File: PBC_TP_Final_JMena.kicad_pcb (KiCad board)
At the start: 2 copper layers, 60 x 96 mm, 146 parts, among them J201 Barrel_Jack, J301 Conn_01x02_Female, J302 Conn_01x02_Female, J303 Conn_01x02_Female, J304 Conn_01x02_Female, J305 Conn_01x02_Female, J306 Conn_01x02_Female, J307 Conn_01x02_Female, J308 Conn_01x02_Female, J501 Conn_01x40_Male, J502 Conn_01x40_Male, J503 Conn_01x06_Male, J504 Conn_01x04, J505 Conn_01x04, J601 USB_B_Micro, J602 DB9_Male, Q401 FDV301N, Q402 FDV301N, Q403 FDV301N, Q404 FDV301N, Q405 FDV301N, Q406 FDV301N, Q407 FDV301N, Q408 FDV301N, Q501 FDV301N, Q502 FDV301N, Q503 FDV301N, Q504 FDV301N, Q505 FDV301N, Q506 FDV301N, Q507 FDV301N, Q508 FDV301N, SW201 SW_DIP_x01, SW401 SW_Push, SW402 SW_Push, SW403 SW_Push, SW404 SW_Push, SW405 SW_Push, SW406 SW_Push, SW407 SW_Push, SW408 SW_Push, U201 NCP1117-5.0_SOT223, U202 LM1084-3.3, U301 LM324, U302 LM324, U303 ADS7828, U304 MCP1525-TT, U601 FT232RL, U602 MAX3232

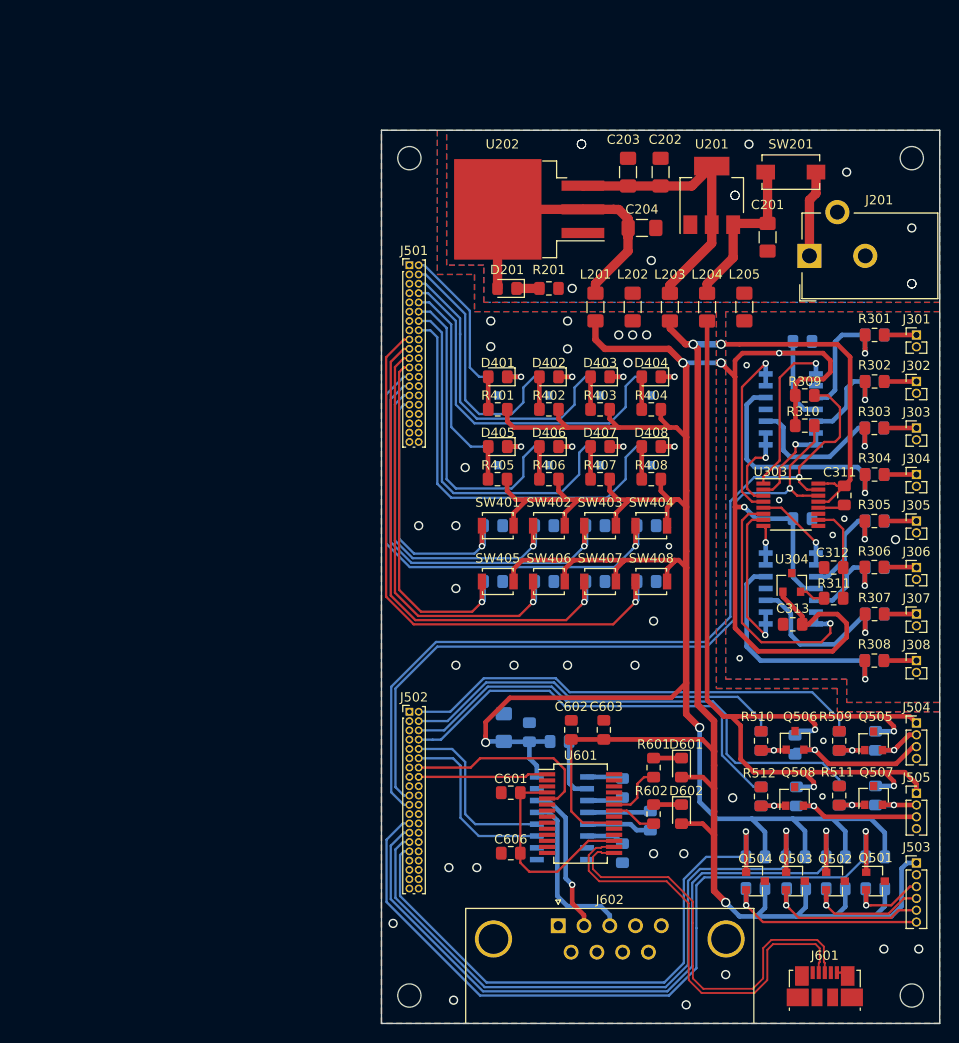
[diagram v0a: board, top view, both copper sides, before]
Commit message: Se realizan correcciones finales y se agregan carpetas BOM, Datasheet, Doc, Gerbers, lib.pretty y shapes3D
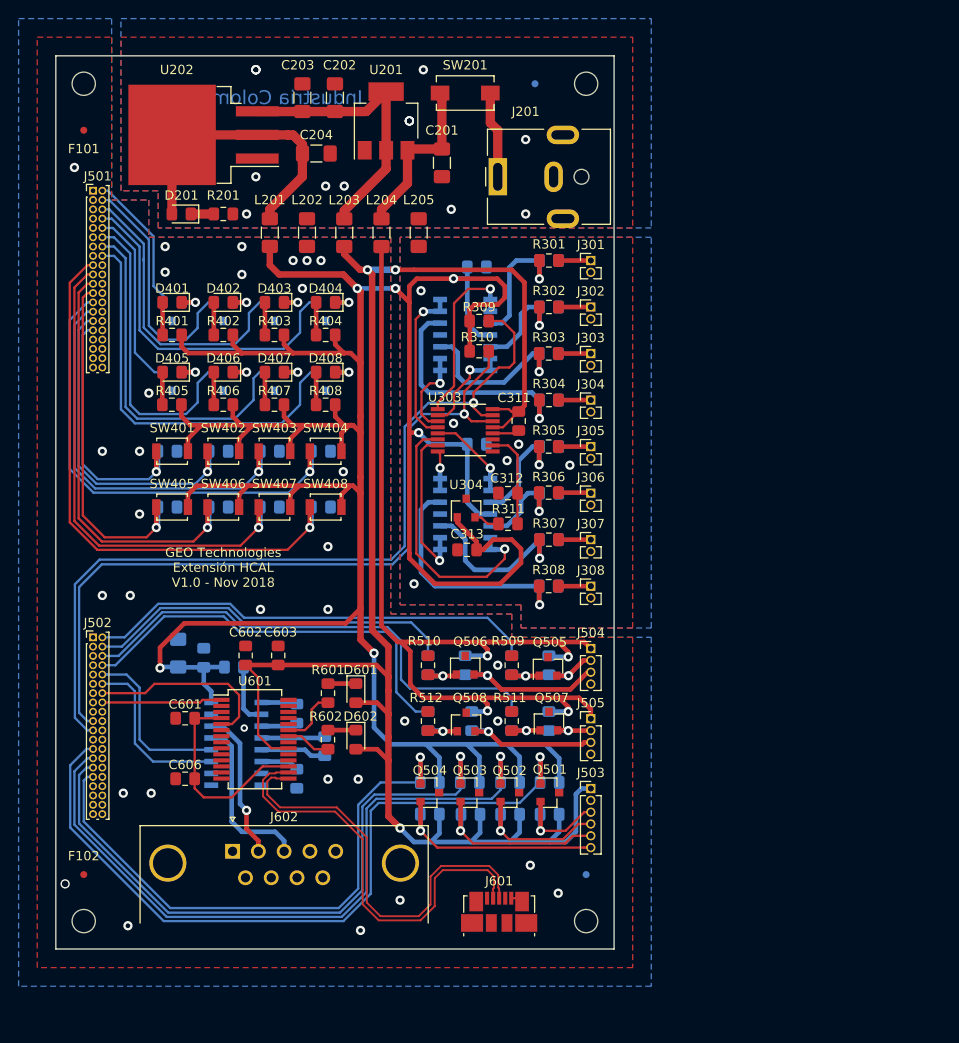
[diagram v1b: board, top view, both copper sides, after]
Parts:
- added F101: Fiducial, Fiducial:Fiducial_0.75mm_Dia_1.5mm_Outer, F.Cu at (82.0, 60.0)
- added F102: Fiducial, Fiducial:Fiducial_0.75mm_Dia_1.5mm_Outer, F.Cu at (82.0, 140.0)
- added F103: Fiducial, Fiducial:Fiducial_0.75mm_Dia_1.5mm_Outer, B.Cu at (130.5, 55.0)
- added F104: Fiducial, Fiducial:Fiducial_0.75mm_Dia_1.5mm_Outer, B.Cu at (136.0, 140.0)
- J201: footprint Connector_BarrelJack:BarrelJack_CUI_PJ-102AH_Horizontal -> Connector_BarrelJack:BarrelJack_CUI_PJ-063AH_Horizontal
- J602: footprint Connector_Dsub:DSUB-9_Male_Horizontal_P2.77x2.84mm_EdgePinOffset7.70mm_Housed_MountingHolesOffset9.12mm -> Connector_Dsub:DSUB-9_Male_Horizontal_P2.77x2.84mm_EdgePinOffset4.94mm_Housed_MountingHolesOffset7.48mm
- moved R506 36.7 mm to (119.0, 117.5)
- moved R510 36.7 mm to (119.0, 117.5)
- moved R508 36.7 mm to (119.0, 123.5)
- moved R512 36.7 mm to (119.0, 123.5)
- moved D506 36.5 mm to (123.0, 117.5)
- moved Q506 36.4 mm to (123.0, 117.5)
- moved Q502 36.3 mm to (127.8, 131.2)
- moved Q501 36.3 mm to (132.1, 131.2)
- moved Q503 36.3 mm to (123.5, 131.2)
- moved Q504 36.3 mm to (119.2, 131.2)
- moved Q508 36.2 mm to (123.1, 123.6)
- moved R505 36.1 mm to (128.0, 117.5)
- moved R509 36.1 mm to (128.0, 117.5)
- moved R507 36.1 mm to (128.0, 123.5)
- moved R511 36.1 mm to (128.0, 123.5)
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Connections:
- net /Comunicación/COMM0 renamed /Comunicación/TXD
- net /Comunicación/COMM1 renamed /Comunicación/RXD
- net /Comunicación/COMM2 renamed /Comunicación/RxIn
- net /Comunicación/COMM3 renamed /Comunicación/TxOut
- net /Conversión Analogo-Digital/I2C0 renamed /Conversión Analogo-Digital/SCL
- net /Conversión Analogo-Digital/I2C1 renamed /Conversión Analogo-Digital/SDA
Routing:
- net /Puertos de Entrada y Salida/PWM1: track 78.2 -> 75.7 mm
- net /Puertos de Entrada y Salida/PWM0: track 84.1 -> 81.6 mm
- net /Puertos de Entrada y Salida/PWM3: track 64.6 -> 62.1 mm
- net /Puertos de Entrada y Salida/PWM2: track 71.8 -> 69.3 mm
- net /Conversión Analogo-Digital/CH3: track 20.0 -> 17.6 mm
- net /Puertos de Entrada y Salida/OP0: track 41.4 -> 39.9 mm
- net /Puertos de Entrada y Salida/PWM_OUT1: track 14.2 -> 15.7 mm
- net /Puertos de Entrada y Salida/PWM_OUT3: track 22.5 -> 24.0 mm
- net /Puertos de Entrada y Salida/PWM_OUT2: track 18.3 -> 19.8 mm
- net /Puertos de Entrada y Salida/PWM_OUT0: track 9.82 -> 11.3 mm
- net /Puertos de Entrada y Salida/CL0: track 49.8 -> 48.7 mm
- net /Conversión Analogo-Digital/CH5: track 28.3 -> 29.4 mm
- net /Puertos de Entrada y Salida/OP1: track 45.7 -> 44.6 mm
- net /Interfaz de Usuario/SW3: track 52.6 -> 51.5 mm
- net /Interfaz de Usuario/LED0: track 16.1 -> 15.1 mm
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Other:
- net class Default: trace_width 0.3 -> 0.25; via_dia 0.5 -> 0.8; via_drill 0.3 -> 0.4
- rule trace_min: 0.1 -> 0.2
- rule via_min_drill: 0.3 -> 0.4
- rule via_min_size: 0.5 -> 0.8
- board text added: "GEO Technologies Extensión HCAL V1.0 - Nov 2018"
- board text added: "Industria Colombiana"
- board text added: "Mínimos (Mayer 10 mils): Grillas: 1mm, 0,5mm, 0,25mm Via: 1 mm / 0,5 mm Márgen: 0,2mm Pista: 1mm, 0.7mm, 0.5mm y 0.25 mm Dist. a borde: 0.2mm Terminación: HASL Recomendaciones del Fabricante Minimo espacio entre Pistas, Vías y Pad: 0.2mm Perforación minima: 0.4mm Minimo Pad componentes - solo vias: 0.25mm Ancho de pista mínimo: 0.2mm Separación al Cobre-Borde: 0.2mm Material: Fibra de Vidrio 1/0 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"
